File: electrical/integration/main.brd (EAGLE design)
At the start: 168 x 104 mm, 115 parts

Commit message: incremental more wires
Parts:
- moved MICROCONTROLLER1:LED1 16.1 mm to (40.1, -62.1)
- moved MICROCONTROLLER1:R1 16.1 mm to (45.5, -62.1)
- moved JETSON1:JETSON_TX2_J21_EXPANSION1:LED1 14.7 mm to (16.8, -38.5)
- moved JETSON1:JETSON_TX2_J21_EXPANSION1:R5 12.3 mm to (31.0, -43.8), turned to 270 degrees
- moved JETSON1:JETSON_TX2_J21_EXPANSION1:LED5 12.3 mm to (31.1, -38.5)
- moved JETSON1:JETSON_TX2_J21_EXPANSION1:R1 12.0 mm to (16.7, -43.8)
- moved MICROCONTROLLER1:LED2 10.1 mm to (40.1, -58.1)
- moved MICROCONTROLLER1:R2 10.1 mm to (45.5, -58.1)
- moved MICROCONTROLLER1:R5 10.0 mm to (45.5, -48.0)
- moved MICROCONTROLLER1:LED5 10.0 mm to (40.1, -48.0)
- moved MICROCONTROLLER1:R4 9.99 mm to (45.5, -50.0)
- moved MICROCONTROLLER1:LED4 9.99 mm to (40.1, -50.0)
- moved MICROCONTROLLER1:LED8 8.09 mm to (40.1, -60.1)
- moved MICROCONTROLLER1:R8 8.09 mm to (45.5, -60.1)
- moved JETSON1:JETSON_TX2_J21_EXPANSION1:LED7 6.48 mm to (22.9, -38.5)
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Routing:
- net N$2: track 0.00 -> 149.6 mm
- net N$6: track 0.00 -> 142.9 mm
- net SENSOR_TOP1:N$4: track 0.00 -> 96.0 mm
- net SENSOR_TOP1:N$3: track 0.00 -> 86.6 mm
- net SENSOR_TOP1:N$1: track 0.00 -> 72.9 mm
- net SENSOR_TOP1:N$2: track 0.00 -> 69.3 mm
- net RELAY_CONTROL_TOP1:N$5: track 0.00 -> 67.8 mm, vias 0 -> 1
- net N$8: track 0.00 -> 57.8 mm
- net N$19: track 0.00 -> 53.8 mm
- net JETSON1:JETSON_TX2_J21_EXPANSION1:VDD_3V3_SYS: track 0.00 -> 50.8 mm
- net N$20: track 0.00 -> 46.3 mm
- net 12V: track 45.4 -> 4.95 mm
- net GND: track 0.00 -> 39.4 mm, vias 0 -> 23
- net RELAY_CONTROL_TOP1:N$11: track 29.5 -> 62.3 mm
- net N$33: track 0.00 -> 32.1 mm
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- added copper zone on layer 1, net 12V
- added copper zone on layer 16, net 12V
- added copper zone on layer 1, net 36V
- added copper zone on layer 16, net GND
- added copper zone on layer 16, net POWER_TOP1:N$2
- added copper zone on layer 16, net RELAY_CONTROL_TOP1:N$1
- added copper zone on layer 1, net RELAY_CONTROL_TOP1:N$11

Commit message: import new dxf
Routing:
- net N$29: track 0.00 -> 86.7 mm
- net N$28: track 0.00 -> 85.9 mm
- net N$30: track 0.00 -> 78.6 mm, vias 0 -> 1
- net N$22: track 0.00 -> 50.6 mm
- net N$21: track 0.00 -> 43.8 mm, vias 0 -> 1
- net N$18: track 0.00 -> 39.0 mm
- net N$3: track 0.00 -> 33.2 mm
- net N$24: track 0.00 -> 30.3 mm
- net N$17: track 0.00 -> 20.6 mm
- net N$13: track 0.00 -> 20.4 mm
- net N$14: track 2.29 -> 18.4 mm
- net RC_INPUT1:SBUS_SIG_IN: track 0.00 -> 6.48 mm, vias 0 -> 1
- net N$15: track 12.3 -> 16.0 mm
- net GND: track 39.4 -> 41.9 mm, vias 23 -> 24
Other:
- outline, holes or cut-outs redrawn

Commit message: incremental
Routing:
- net RELAY_CONTROL_TOP1:36V_RAW: track 40.6 -> 145.2 mm, vias 2 -> 3
- net SENSOR_TOP1:N$1: track 72.9 -> 0.00 mm
- net N$4: track 0.00 -> 64.7 mm, vias 0 -> 2
- net N$12: track 2.60 -> 59.4 mm
- net N$8: track 57.8 -> 95.5 mm
- net N$28: track 85.9 -> 121.9 mm, vias 0 -> 1
- net N$29: track 86.7 -> 116.2 mm, vias 0 -> 1
- net N$30: track 78.6 -> 101.6 mm
- net 5V: track 31.6 -> 51.7 mm
- net SENSOR_TOP1:N$2: track 69.3 -> 55.7 mm
- net MICROCONTROLLER1:LED_SDA: track 0.00 -> 11.5 mm
- net RELAY_CONTROL_TOP1:N$2: track 14.2 -> 21.8 mm, vias 0 -> 1
- net RELAY_CONTROL_TOP1:N$4: track 4.38 -> 9.78 mm, vias 0 -> 1
- net N$2: track 149.6 -> 144.8 mm
- net RELAY_CONTROL_TOP1:ISO1:N$4: track 0.00 -> 2.77 mm
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
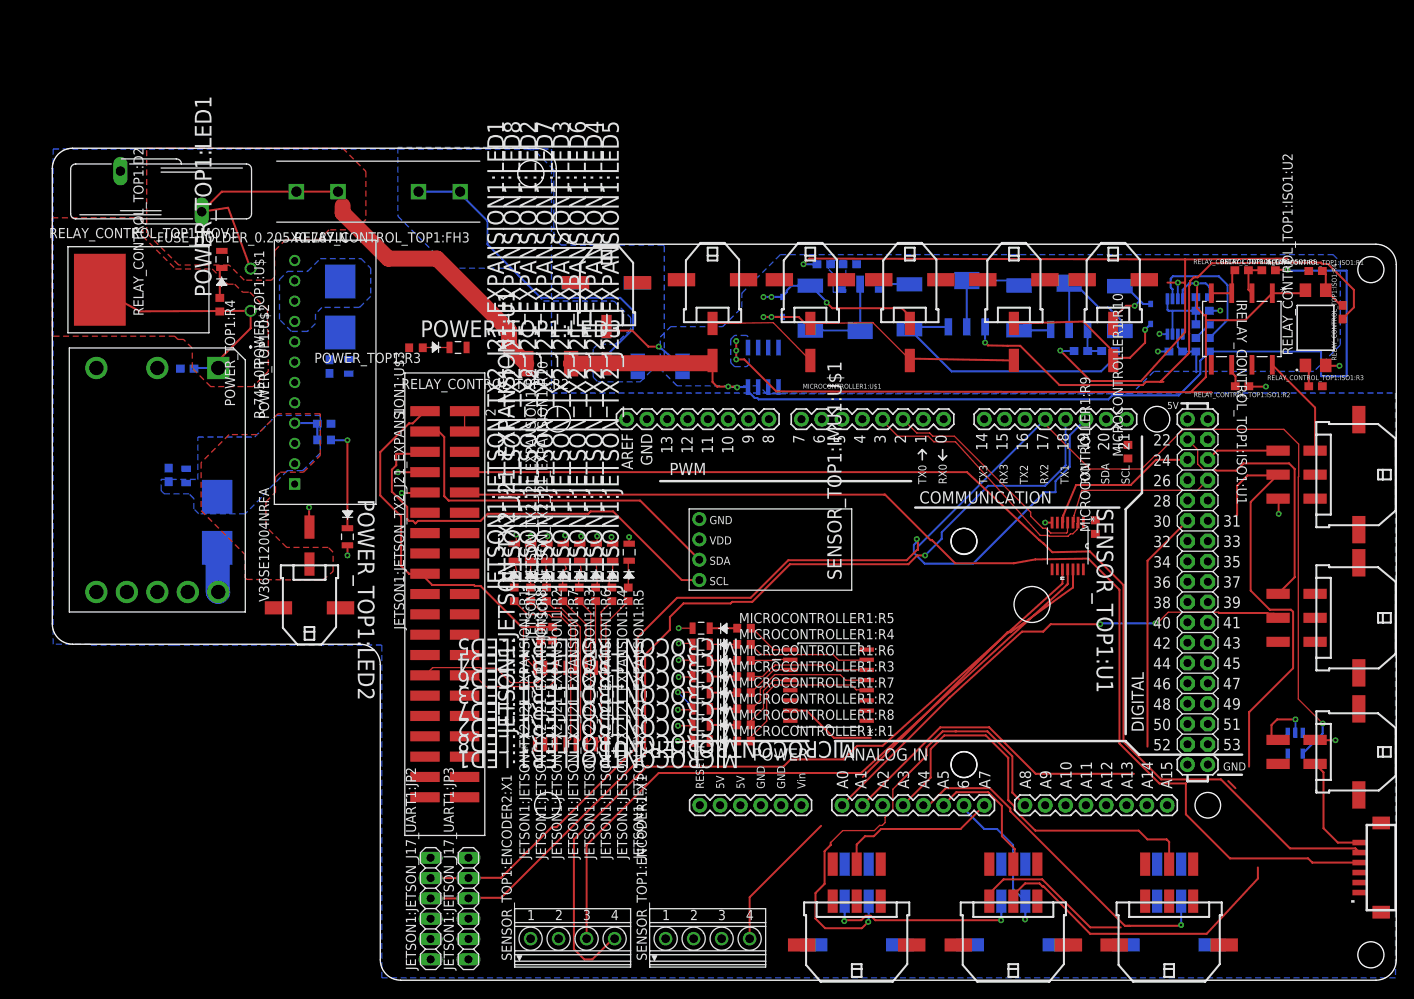
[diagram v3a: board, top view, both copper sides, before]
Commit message: connected non-pwr signals
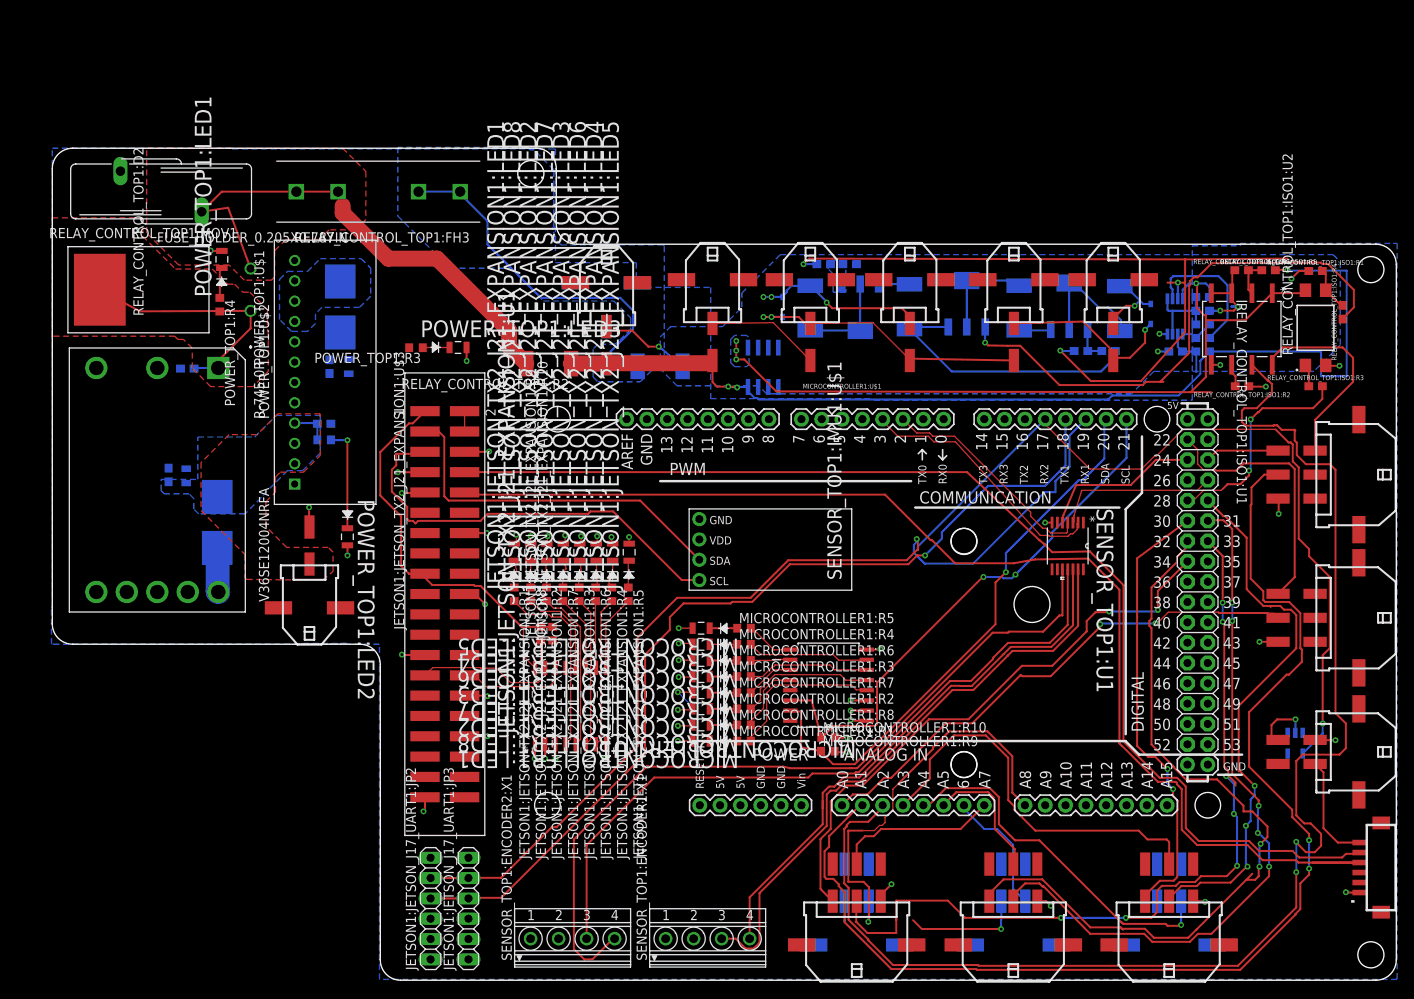
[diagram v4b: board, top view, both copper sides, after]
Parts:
- moved MICROCONTROLLER1:R10 51.8 mm to (56.0, -61.7), turned to 0 degrees
- moved MICROCONTROLLER1:R9 43.6 mm to (55.9, -63.4), turned to 0 degrees
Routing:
- net VSENSE: track 0.00 -> 172.8 mm, vias 0 -> 2
- net N$9: track 0.00 -> 104.2 mm, vias 0 -> 7
- net N$17: track 20.6 -> 96.4 mm, vias 0 -> 2
- net SENSOR_TOP1:N$1: track 0.00 -> 74.8 mm
- net N$10: track 0.00 -> 72.9 mm, vias 0 -> 2
- net MICROCONTROLLER1:LED_SCL: track 0.00 -> 68.9 mm, vias 0 -> 2
- net N$25: track 0.00 -> 68.6 mm, vias 0 -> 3
- net MICROCONTROLLER1:LED_SDA: track 11.5 -> 69.9 mm, vias 0 -> 1
- net N$8: track 95.5 -> 149.0 mm, vias 0 -> 2
- net N$18: track 39.0 -> 88.8 mm, vias 0 -> 5
- net GND: track 41.9 -> 90.7 mm, vias 24 -> 47
- net MOW_EN: track 0.00 -> 27.7 mm, vias 0 -> 2
- net N$24: track 30.3 -> 56.0 mm, vias 0 -> 2
- net SENSOR_TOP1:N$2: track 55.7 -> 69.9 mm
- net GND_ISO: track 55.3 -> 64.7 mm, vias 4 -> 6
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
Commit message: sweeeet 5V polygonzzzz
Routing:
- net RELAY_CONTROL_TOP1:RELAY_CONTROL1:!UVLO!: track 97.5 -> 84.7 mm
- net VSENSE: track 172.8 -> 167.8 mm
- net N$30: track 101.9 -> 105.4 mm
- net 5V: track 55.9 -> 52.4 mm, vias 1 -> 17
- net GND: track 90.7 -> 91.9 mm
- added copper zone on layer 1, net 5V
- added copper zone on layer 16, net 5V

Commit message: 12V polygon
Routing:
- net RELAY_CONTROL_TOP1:N$1: track 42.8 -> 0.00 mm
- net 36V: track 30.8 -> 0.00 mm
- net RELAY_CONTROL_TOP1:N$11: track 62.3 -> 38.0 mm
- net SENSOR_TOP1:N$4: track 99.0 -> 97.2 mm
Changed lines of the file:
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@@
 <vertex x="-7.7" y="-42"/>
 </polygon>
-<wire x1="-8.85" y1="-39.98" x2="52.64" y2="-70.13" width="0" layer="19" extent="1-1"/>
+<polygon width="0.25" layer="1">
+<vertex x="-10.8" y="-37.8"/>
+<vertex x="-10.8" y="-49.9"/>
+<vertex x="-0.1" y="-49.9"/>
+<vertex x="-0.1" y="-91.9"/>
+<vertex x="38" y="-91.9"/>
+<vertex x="38" y="-80.1"/>
+<vertex x="41.5" y="-76.6"/>
+<vertex x="49.6" y="-76.6"/>
+<vertex x="54" y="-72.2"/>
+<vertex x="54" y="-67.8"/>
+<vertex x="53.5" y="-67.3"/>
+<vertex x="35.5" y="-67.3"/>
+<vertex x="32" y="-70.8"/>
+<vertex x="32" y="-88.3"/>
+<vertex x="17.4" y="-88.3"/>
+<vertex x="17.4" y="-83"/>
+<vertex x="4.7" y="-83"/>
+<vertex x="4.3" y="-37.8"/>
+</polygon>
 </signal>
 <signal name="MICROCONTROLLER1:AREF">
@@
 <contactref element="RELAY_CONTROL_TOP1:D2" pad="1"/>
 <contactref element="RELAY_CONTROL_TOP1:D2" pad="2"/>
-<wire x1="-35.0552" y1="-5.69" x2="-30.0516" y2="-8.39" width="0.25" layer="1"/>
-<wire x1="-30.0516" y1="-8.39" x2="-16.2084" y2="-8.3332" width="0.25" layer="1"/>
-<wire x1="-16.2084" y1="-8.3332" x2="-16.2084" y2="-10.5084" width="0.25" layer="1"/>
-<wire x1="-16.2084" y1="-10.5084" x2="-20.5" y2="-14.8" width="0.25" layer="1"/>
 <polygon width="0.25" layer="1">
 <vertex x="-41" y="3.3"/>
@@
 <vertex x="-41" y="-11.5"/>
 </polygon>
-<wire x1="-23.28" y1="-15.55" x2="-23.2" y2="-15.47" width="0.25" layer="16"/>
-<wire x1="-23.2" y1="-15.47" x2="-20.25" y2="-15.47" width="0.25" layer="16"/>
+<wire x1="-20.25" y1="-15.47" x2="-23.28" y2="-15.55" width="0" layer="19" extent="16-16"/>
 </signal>
 <signal name="POWER_TOP1:N$1">
@@
 <contactref element="SENSOR_TOP1:ENCODER2:X1" pad="4"/>
 <contactref element="SENSOR_TOP1:U1" pad="10"/>
-<wire x1="29.29" y1="-86.81" x2="29.09" y2="-86.81" width="0.25" layer="1"/>
-<wire x1="29.09" y1="-86.81" x2="26.5" y2="-89.4" width="0.25" layer="1"/>
-<wire x1="26.5" y1="-89.4" x2="25.5" y2="-89.4" width="0.25" layer="1"/>
-<wire x1="25.5" y1="-89.4" x2="24.2" y2="-88.1" width="0.25" layer="1"/>
-<wire x1="24.2" y1="-88.1" x2="24.2" y2="-74.4" width="0.25" layer="1"/>
+<wire x1="24.2" y1="-84.4" x2="24.2" y2="-74.4" width="0.25" layer="1"/>
 <wire x1="33.4" y1="-65.2" x2="33.5" y2="-65.3" width="0.25" layer="1"/>
 <wire x1="33.5" y1="-65.3" x2="50.4" y2="-65.3" width="0.25" layer="1"/>
@@
 <wire x1="78.465421875" y1="-48.556384375" x2="78.6" y2="-48.42180625" width="0.25" layer="1"/>
 <wire x1="59.61276875" y1="-65.5" x2="76.556384375" y2="-48.556384375" width="0.25" layer="1"/>
+<wire x1="26.29906875" y1="-88.039" x2="25.28093125" y2="-88.039" width="0.25" layer="1"/>
+<wire x1="25.28093125" y1="-88.039" x2="24.561" y2="-87.31906875" width="0.25" layer="1"/>
+<wire x1="29.29" y1="-86.81" x2="27.52806875" y2="-86.81" width="0.25" layer="1"/>
+<wire x1="27.52806875" y1="-86.81" x2="26.29906875" y2="-88.039" width="0.25" layer="1"/>
+<wire x1="24.561" y1="-84.761" x2="24.2" y2="-84.4" width="0.25" layer="1"/>
+<wire x1="24.561" y1="-87.31906875" x2="24.561" y2="-84.761" width="0.25" layer="1"/>
 </signal>
 <signal name="RELAY_CONTROL_TOP1:ISO1:N$1">
@@
 <contactref element="RELAY_CONTROL_TOP1:MOV1" pad="1"/>
 <wire x1="-5.2792" y1="6.57" x2="-10.4862" y2="6.57" width="0.25" layer="1"/>
-<wire x1="-10.4862" y1="6.57" x2="-19.81" y2="6.57" width="0.25" layer="1"/>
-<wire x1="-19.81" y1="6.57" x2="-22.32" y2="4.06" width="0.25" layer="1"/>
-<wire x1="-22.32" y1="4.06" x2="-19.02" y2="4.5616" width="0.25" layer="1"/>
-<wire x1="-19.02" y1="4.5616" x2="-16.2084" y2="-3.05" width="0.25" layer="1"/>
 <polygon width="0.25" layer="1">
 <vertex x="-26.3" y="12"/>
@@
 <contactref element="RELAY_CONTROL_TOP1:FH3" pad="2"/>
 <contactref element="RELAY_CONTROL_TOP1:JBAT" pad="P$2"/>
-<wire x1="4.7792" y1="6.57" x2="9.73" y2="6.57" width="0.25" layer="16"/>
-<wire x1="9.73" y1="6.57" x2="13.4" y2="2.9" width="0.25" layer="16"/>
-<wire x1="13.4" y1="-0.02" x2="13.4" y2="2.9" width="0.25" layer="16"/>
-<wire x1="28.25" y1="-14.935" x2="28.15" y2="-14.05" width="0.25" layer="16"/>
-<wire x1="28.15" y1="-14.05" x2="31.6" y2="-10.6" width="0.25" layer="16"/>
-<wire x1="31.6" y1="-10.6" x2="31.6" y2="-8.3" width="0.25" layer="16"/>
-<wire x1="31.6" y1="-8.3" x2="30" y2="-6.7" width="0.25" layer="16"/>
-<wire x1="30" y1="-6.7" x2="20.08" y2="-6.7" width="0.25" layer="16"/>
-<wire x1="20.08" y1="-6.7" x2="13.4" y2="-0.02" width="0.25" layer="16"/>
 <polygon width="0.25" layer="16">
 <vertex x="2.2" y="12.1"/>

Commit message: all connected
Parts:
- moved RC_INPUT1:U1 5.74 mm to (114.4, -56.6), turned to 90 degrees
- moved RELAY_CONTROL_TOP1:R1 3.80 mm to (38.8, -15.5), turned to 270 degrees
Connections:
- removed net MICROCONTROLLER1:5V: MICROCONTROLLER1:U$1.5V@0, MICROCONTROLLER1:U$1.5V@1, MICROCONTROLLER1:U$1.5V@2
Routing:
- net 3V3: track 3.35 -> 159.6 mm, vias 2 -> 7
- net 5V: track 52.4 -> 128.4 mm, vias 17 -> 18
- net GND_ISO: track 64.7 -> 34.3 mm
- net N$30: track 105.4 -> 79.1 mm
- net VSENSE: track 167.8 -> 178.6 mm
- net RELAY_CONTROL_TOP1:N$4: track 9.78 -> 17.9 mm
- net RELAY_CONTROL_TOP1:N$6: track 21.7 -> 29.7 mm
- net N$31: track 28.0 -> 36.0 mm
- net RELAY_CONTROL_TOP1:36V_RAW: track 145.2 -> 138.0 mm
- net N$33: track 32.1 -> 37.7 mm
- net N$2: track 151.5 -> 157.0 mm
- net GND: track 91.9 -> 97.1 mm
- net N$6: track 146.5 -> 151.6 mm
- net N$29: track 116.2 -> 120.0 mm, vias 1 -> 2
- net MICROCONTROLLER1:LED_SCL: track 68.9 -> 72.3 mm
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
